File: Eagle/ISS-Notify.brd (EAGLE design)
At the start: 63.5 x 63.5 mm, 56 parts, among them J3 PROTOSPACE2, SW1 9077-1, U1 ATMEGA32U4, U2 MCP7940N, U3 TPS63001, U4 MCP73811, U5 TLC5971, U6 TLC5971, X1 8 MHz, X2 32.768 kHz

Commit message: test pin placement on board
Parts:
- added TESTCLOCK, TESTDATA, TESTGND, TESTSCL, TESTSDC, TESTVBAT: TESTPIN, ISS-Notify:TESTPIN
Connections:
- net GND: now also TESTGND.P$1
- net LED_CLK: now also TESTCLOCK.P$1
- net LED_DATA: now also TESTDATA.P$1
- net SCL: now also TESTSCL.P$1
- net SDA: now also TESTSDC.P$1
- net VBAT: now also TESTVBAT.P$1
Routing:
- net LED_CLK: track 10.9 -> 18.2 mm, vias 0 -> 2
- net SCL: track 27.4 -> 31.3 mm
- net LED_DATA: track 13.7 -> 17.4 mm
- net VBAT: track 16.9 -> 20.2 mm
- net SDA: track 26.5 -> 27.4 mm
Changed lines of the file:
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@@
 <attribute name="VALUE" x="48" y="62.5" size="1" layer="27" ratio="10" rot="R180"/>
 </element>
+<element name="TESTVBAT" library="ISS-Notify" package="TESTPIN" value="TESTPIN" x="44.5" y="58.3"/>
+<element name="TESTSCL" library="ISS-Notify" package="TESTPIN" value="TESTPIN" x="36.2" y="10"/>
+<element name="TESTSDC" library="ISS-Notify" package="TESTPIN" value="TESTPIN" x="46.1" y="13.4"/>
+<element name="TESTDATA" library="ISS-Notify" package="TESTPIN" value="TESTPIN" x="27.3" y="44.8"/>
+<element name="TESTCLOCK" library="ISS-Notify" package="TESTPIN" value="TESTPIN" x="27.3" y="47.1"/>
+<element name="TESTGND" library="ISS-Notify" package="TESTPIN" value="TESTPIN" x="57" y="8.9"/>
 </elements>
 <signals>
@@
 <wire x1="15.51" y1="55.625" x2="15.51" y2="53.69" width="0.254" layer="1"/>
 <wire x1="15.51" y1="53.69" x2="15.7" y2="53.5" width="0.254" layer="1"/>
+<contactref element="TESTGND" pad="P$1"/>
 <wire x1="13.46" y1="57.35" x2="13.4239" y2="57.3405" width="0" layer="19" extent="1-1"/>
 <wire x1="16.56" y1="57.35" x2="16.5354" y2="57.3405" width="0" layer="19" extent="1-1"/>
@@
 <wire x1="32.5" y1="24.7" x2="32.5" y2="25.7" width="0.254" layer="1"/>
 <wire x1="32.5" y1="25.7" x2="32.55" y2="25.75" width="0.254" layer="1"/>
+<contactref element="TESTSCL" pad="P$1"/>
+<wire x1="36.2" y1="10" x2="35.6" y2="10" width="0.254" layer="1"/>
+<wire x1="35.6" y1="10" x2="33.7" y2="11.9" width="0.254" layer="1"/>
+<wire x1="33.7" y1="11.9" x2="33.7" y2="12.1" width="0.254" layer="1"/>
+<wire x1="33.7" y1="12.1" x2="33.4" y2="12.4" width="0.254" layer="1"/>
 </signal>
 <signal name="SDA">
@@
 <wire x1="33.5" y1="14" x2="33.3" y2="13.8" width="0.254" layer="16"/>
 <wire x1="33.3" y1="13.8" x2="33.3" y2="13.3" width="0.254" layer="16"/>
+<contactref element="TESTSDC" pad="P$1"/>
+<wire x1="45.425" y1="12.775" x2="45.475" y2="12.775" width="0.254" layer="1"/>
+<wire x1="45.475" y1="12.775" x2="46.1" y2="13.4" width="0.254" layer="1"/>
 </signal>
 <signal name="N$10">
@@
 <wire x1="47.86" y1="58.2" x2="47.9" y2="59.3" width="0.6096" layer="1"/>
 <wire x1="47.9" y1="59.3" x2="47.9" y2="60.5" width="0.6096" layer="1"/>
+<contactref element="TESTVBAT" pad="P$1"/>
+<wire x1="47.81" y1="58.25" x2="44.75" y2="58.25" width="0.6096" layer="1"/>
+<wire x1="44.75" y1="58.25" x2="44.5" y2="58.3" width="0.6096" layer="1"/>
 </signal>
 <signal name="N$15">
@@
 <wire x1="34.385" y1="45.985" x2="34.3" y2="45.9" width="0.254" layer="1"/>
 <wire x1="34.3" y1="45.9" x2="32.9" y2="45.9" width="0.254" layer="1"/>
-<wire x1="32.9" y1="45.9" x2="29.4" y2="42.4" width="0.254" layer="1"/>
+<wire x1="32.9" y1="45.9" x2="30.55" y2="43.55" width="0.254" layer="1"/>
+<contactref element="TESTDATA" pad="P$1"/>
+<wire x1="30.55" y1="43.55" x2="29.4" y2="42.4" width="0.254" layer="1"/>
+<wire x1="27.3" y1="44.8" x2="29.3" y2="44.8" width="0.254" layer="1"/>
+<wire x1="29.3" y1="44.8" x2="30.55" y2="43.55" width="0.254" layer="1"/>
 </signal>
 <signal name="LED_CLK">
@@
 <contactref element="U1" pad="41"/>
 <wire x1="30.15" y1="37.75" x2="30.15" y2="42.15" width="0.254" layer="1"/>
-<wire x1="30.15" y1="42.15" x2="33.3" y2="45.3" width="0.254" layer="1"/>
+<wire x1="30.15" y1="42.15" x2="31.35" y2="43.35" width="0.254" layer="1"/>
+<wire x1="31.35" y1="43.35" x2="33.3" y2="45.3" width="0.254" layer="1"/>
 <wire x1="33.3" y1="45.3" x2="35.265" y2="45.3" width="0.254" layer="1"/>
 <wire x1="35.265" y1="45.3" x2="35.3" y2="45.335" width="0.254" layer="1"/>
+<contactref element="TESTCLOCK" pad="P$1"/>
+<wire x1="27.3" y1="47.1" x2="30.6" y2="47.1" width="0.254" layer="1"/>
+<wire x1="30.6" y1="47.1" x2="31.3" y2="46.4" width="0.254" layer="1"/>
+<via x="31.3" y="46.4" extent="1-16" drill="0.36"/>
+<wire x1="31.3" y1="46.4" x2="31.3" y2="43.4" width="0.254" layer="16"/>
+<wire x1="31.3" y1="43.4" x2="31.35" y2="43.35" width="0.254" layer="16"/>
+<via x="31.35" y="43.35" extent="1-16" drill="0.36"/>
 </signal>
 <signal name="N$17">

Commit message: incrament board version on screen
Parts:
- U$5: value V0.3 -> V0.4
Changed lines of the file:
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@@
 <attribute name="VALUE" x="50.36" y="7.666" size="1" layer="27" ratio="10" rot="R90"/>
 </element>
-<element name="U$5" library="ISS-Notify" package="LOGO" value="V0.3" x="40.7" y="35.5"/>
+<element name="U$5" library="ISS-Notify" package="LOGO" value="V0.4" x="40.7" y="35.5"/>
 <element name="C17" library="rcl_custom" package="0603-C-NOSILK" value="1 uF" x="47.2" y="60.5" smashed="yes" rot="R180">
 <attribute name="NAME" x="51" y="61.15" size="0.8" layer="25" font="vector" ratio="20" rot="R180"/>

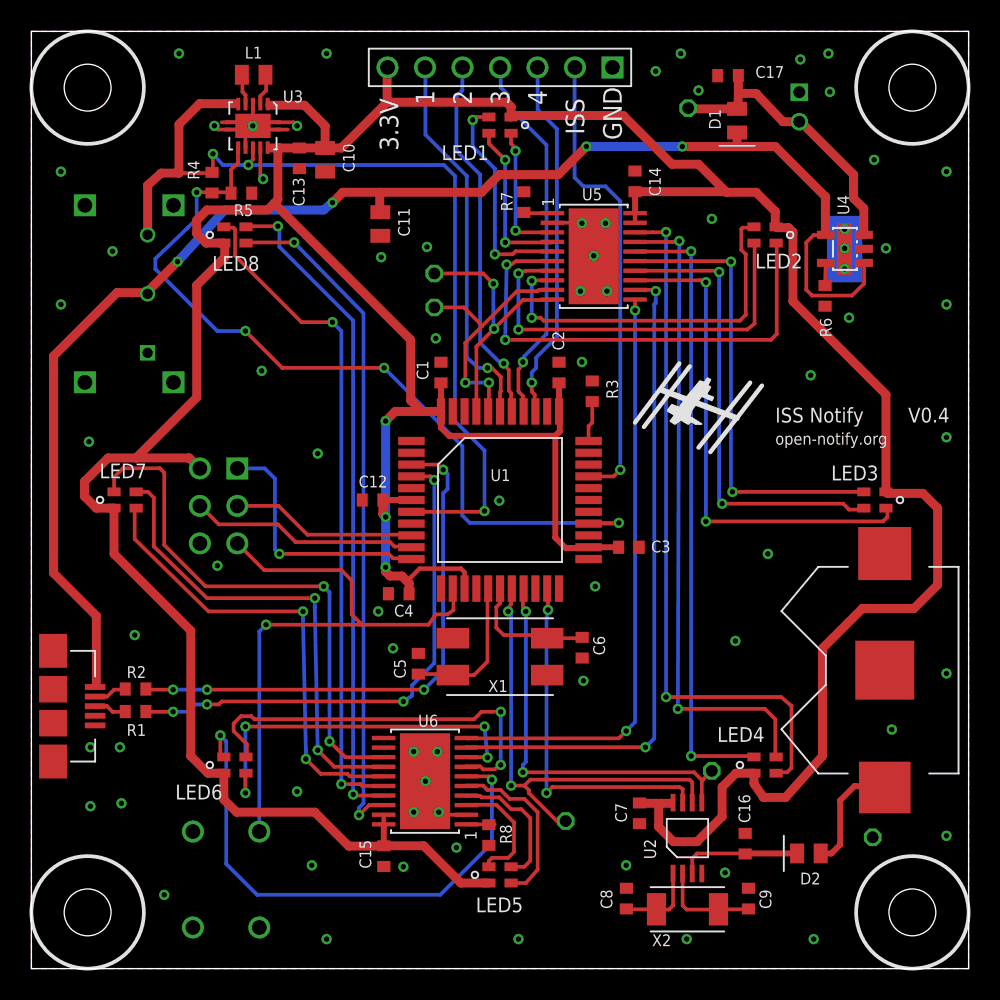
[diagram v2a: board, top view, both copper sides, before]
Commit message: fixed annoying bolt landing, moved a via or two
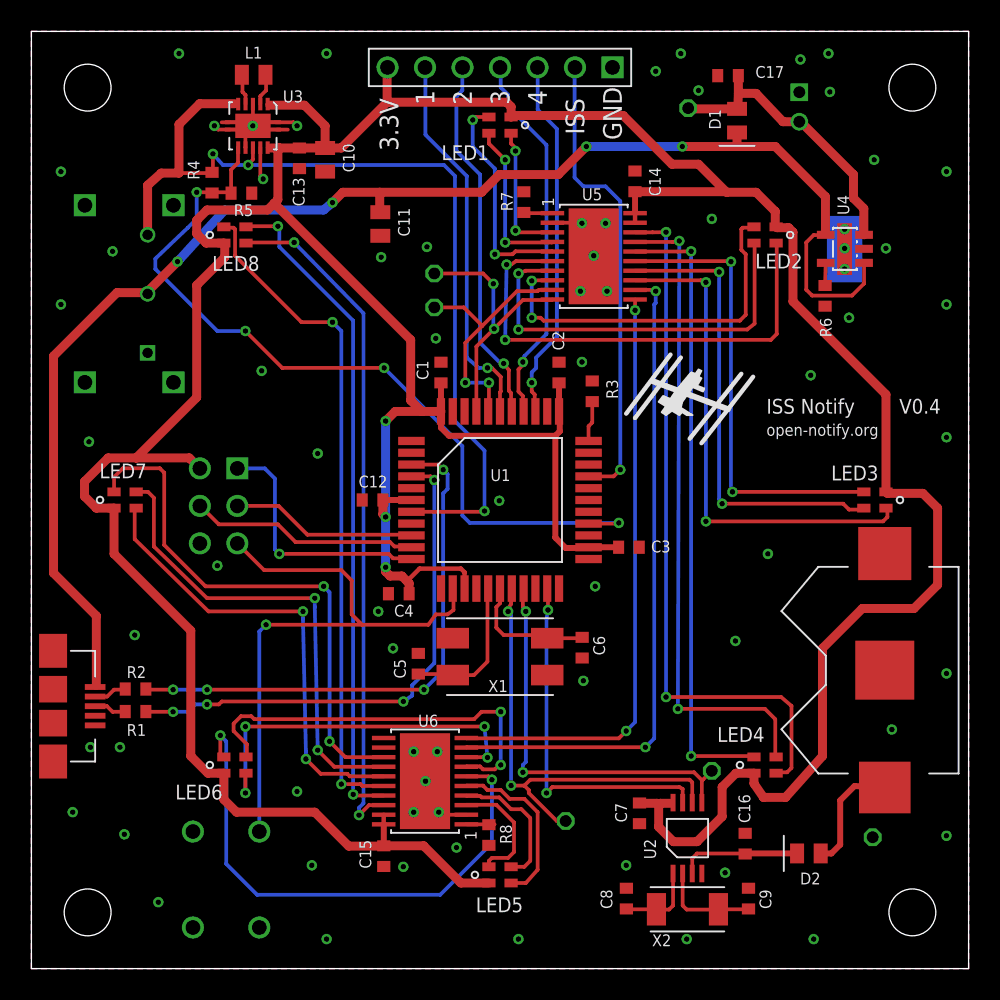
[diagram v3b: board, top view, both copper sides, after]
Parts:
- U$1, U$2, U$3, U$4: value _4-BARE_MOUNTING_HOLE/.300 -> _4-BARE_MOUNTING_HOLE/.250; device ISS-Notify:_4/.300-BARE+STD_NUT_OR_STAR_WASHER -> ISS-Notify:_4/.250-BARE+STD_WASHER
- moved U$5 0.85 mm to (40.1, 36.1)
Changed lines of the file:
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@@
 <layer number="39" name="tKeepout" color="4" fill="11" visible="no" active="yes"/>
 <layer number="40" name="bKeepout" color="1" fill="11" visible="no" active="yes"/>
-<layer number="41" name="tRestrict" color="4" fill="10" visible="no" active="yes"/>
+<layer number="41" name="tRestrict" color="4" fill="10" visible="yes" active="yes"/>
 <layer number="42" name="bRestrict" color="1" fill="10" visible="no" active="yes"/>
 <layer number="43" name="vRestrict" color="2" fill="10" visible="no" active="yes"/>
@@
 <layer number="46" name="Milling" color="3" fill="1" visible="no" active="yes"/>
 <layer number="47" name="Measures" color="7" fill="1" visible="no" active="yes"/>
-<layer number="48" name="Document" color="7" fill="1" visible="yes" active="yes"/>
+<layer number="48" name="Document" color="7" fill="1" visible="no" active="yes"/>
 <layer number="49" name="Reference" color="7" fill="1" visible="no" active="yes"/>
 <layer number="50" name="dxf" color="7" fill="1" visible="no" active="no"/>
-<layer number="51" name="tDocu" color="7" fill="1" visible="yes" active="yes"/>
+<layer number="51" name="tDocu" color="7" fill="1" visible="no" active="yes"/>
 <layer number="52" name="bDocu" color="7" fill="1" visible="no" active="yes"/>
 <layer number="53" name="tGND_GNDA" color="7" fill="1" visible="no" active="no"/>
@@
 <attribute name="NAME" x="17.008" y="3.364" size="1.27" layer="26" font="vector" ratio="20" rot="MR90"/>
 </element>
-<element name="U$1" library="ISS-Notify" package="_4/.300-BARE+STD_NUT_OR_STAR_WASHER" value="_4-BARE_MOUNTING_HOLE/.300" x="3.81" y="59.69" smashed="yes">
+<element name="U$1" library="ISS-Notify" package="_4/.250-BARE+STD_WASHER" value="_4-BARE_MOUNTING_HOLE/.250" x="3.81" y="59.69" smashed="yes">
 <attribute name="VALUE" x="6.985" y="56.515" size="1.27" layer="27"/>
 </element>
-<element name="U$2" library="ISS-Notify" package="_4/.300-BARE+STD_NUT_OR_STAR_WASHER" value="_4-BARE_MOUNTING_HOLE/.300" x="59.69" y="59.69" smashed="yes">
+<element name="U$2" library="ISS-Notify" package="_4/.250-BARE+STD_WASHER" value="_4-BARE_MOUNTING_HOLE/.250" x="59.69" y="59.69" smashed="yes">
 <attribute name="VALUE" x="62.865" y="56.515" size="1.27" layer="27"/>
 </element>
-<element name="U$3" library="ISS-Notify" package="_4/.300-BARE+STD_NUT_OR_STAR_WASHER" value="_4-BARE_MOUNTING_HOLE/.300" x="59.69" y="3.81" smashed="yes">
+<element name="U$3" library="ISS-Notify" package="_4/.250-BARE+STD_WASHER" value="_4-BARE_MOUNTING_HOLE/.250" x="59.69" y="3.81" smashed="yes">
 <attribute name="VALUE" x="62.865" y="0.635" size="1.27" layer="27"/>
 </element>
-<element name="U$4" library="ISS-Notify" package="_4/.300-BARE+STD_NUT_OR_STAR_WASHER" value="_4-BARE_MOUNTING_HOLE/.300" x="3.81" y="3.81" smashed="yes">
+<element name="U$4" library="ISS-Notify" package="_4/.250-BARE+STD_WASHER" value="_4-BARE_MOUNTING_HOLE/.250" x="3.81" y="3.81" smashed="yes">
 <attribute name="VALUE" x="6.985" y="0.635" size="1.27" layer="27"/>
 </element>
@@
 <attribute name="VALUE" x="50.36" y="7.666" size="1" layer="27" ratio="10" rot="R90"/>
 </element>
-<element name="U$5" library="ISS-Notify" package="LOGO" value="V0.4" x="40.7" y="35.5"/>
+<element name="U$5" library="ISS-Notify" package="LOGO" value="V0.4" x="40.1" y="36.1"/>
 <element name="C17" library="rcl_custom" package="0603-C-NOSILK" value="1 uF" x="47.2" y="60.5" smashed="yes" rot="R180">
 <attribute name="NAME" x="51" y="61.15" size="0.8" layer="25" font="vector" ratio="20" rot="R180"/>
@@
 <via x="4" y="15" extent="1-16" drill="0.36"/>
 <via x="6" y="15" extent="1-16" drill="0.36"/>
-<via x="4" y="11" extent="1-16" drill="0.36"/>
+<via x="2.8" y="10.6" extent="1-16" drill="0.36"/>
 <via x="19" y="7" extent="1-16" drill="0.36"/>
 <via x="18" y="12" extent="1-16" drill="0.36"/>
@@
 <via x="19.4" y="34.9" extent="1-16" drill="0.36"/>
 <via x="7" y="22.6" extent="1-16" drill="0.36"/>
-<via x="6.1" y="11.2" extent="1-16" drill="0.36"/>
+<via x="6.3" y="9.1" extent="1-16" drill="0.36"/>
 <via x="38.1" y="48.3" extent="1-16" drill="0.36"/>
 <via x="57.1" y="54.8" extent="1-16" drill="0.36"/>
@@
 <via x="62" y="20" extent="1-16" drill="0.36"/>
 <via x="62" y="9" extent="1-16" drill="0.36"/>
-<via x="9" y="5" extent="1-16" drill="0.36"/>
+<via x="8.6" y="4.5" extent="1-16" drill="0.36"/>
 <contactref element="C11" pad="2"/>
 <contactref element="C17" pad="2"/>
@@
 </signal>
 </signals>
-<errors>
-</errors>
 </board>
 </drawing>

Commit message: Fixed L1 packages, changed USB header. Passes ERC, DRC, rats. Ship it.
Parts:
- removed USB: CON_USB-MICRO-6GND, ISS-Notify:USBMICROSMT
- added J1: ZX62D-B-5P8, con-hirose-microusb:ZX62D-B-5P8
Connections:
- net GND: now also J1.P$1, J1.P$2, J1.P$3, J1.P$4, J1.P5, U1.42; no longer USB.5
- net N$4: now also J1.P3; no longer USB.D+
- net N$5: now also J1.P2; no longer USB.D-
- net VUSB: now also J1.P1; no longer USB.VUSB
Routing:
- net VUSB: track 99.1 -> 100.6 mm
- net GND: track 16.2 -> 16.3 mm, vias 67 -> 65

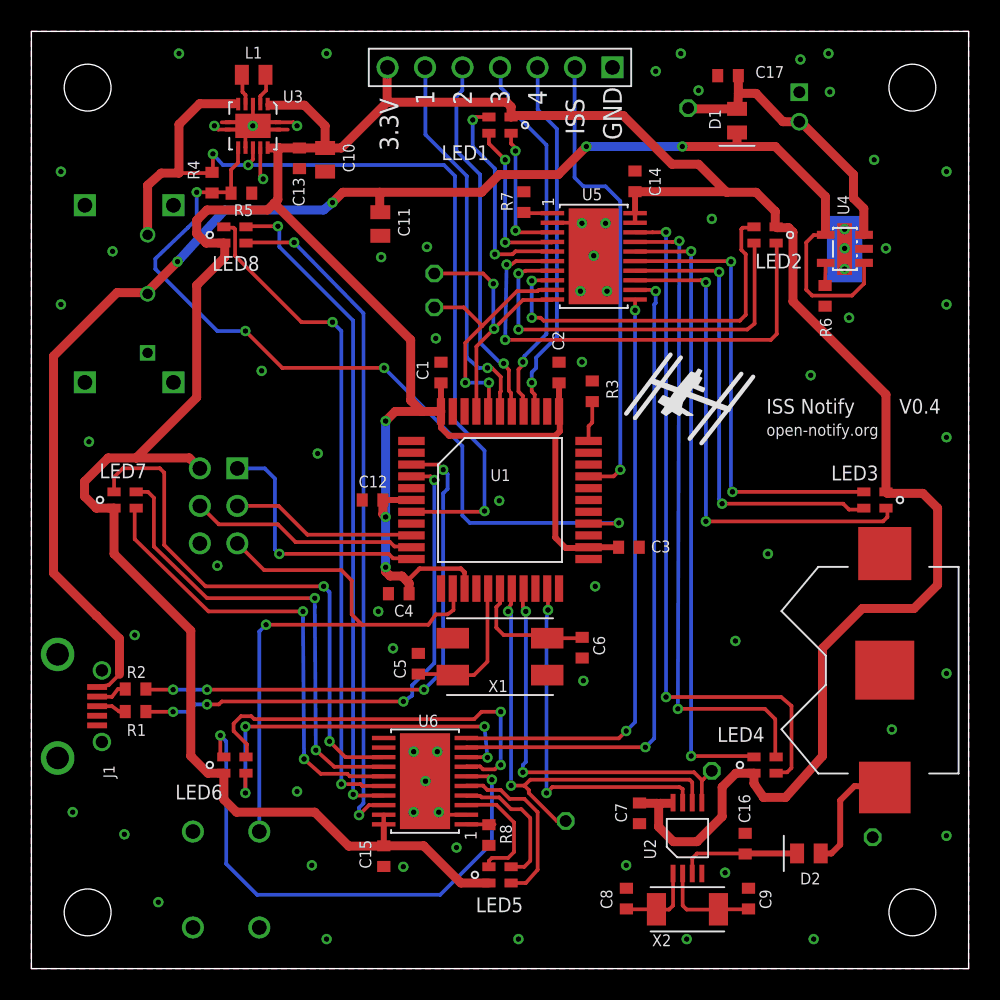
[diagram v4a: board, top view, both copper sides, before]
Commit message: Added fiducials per Screaming Circuits blog postw.
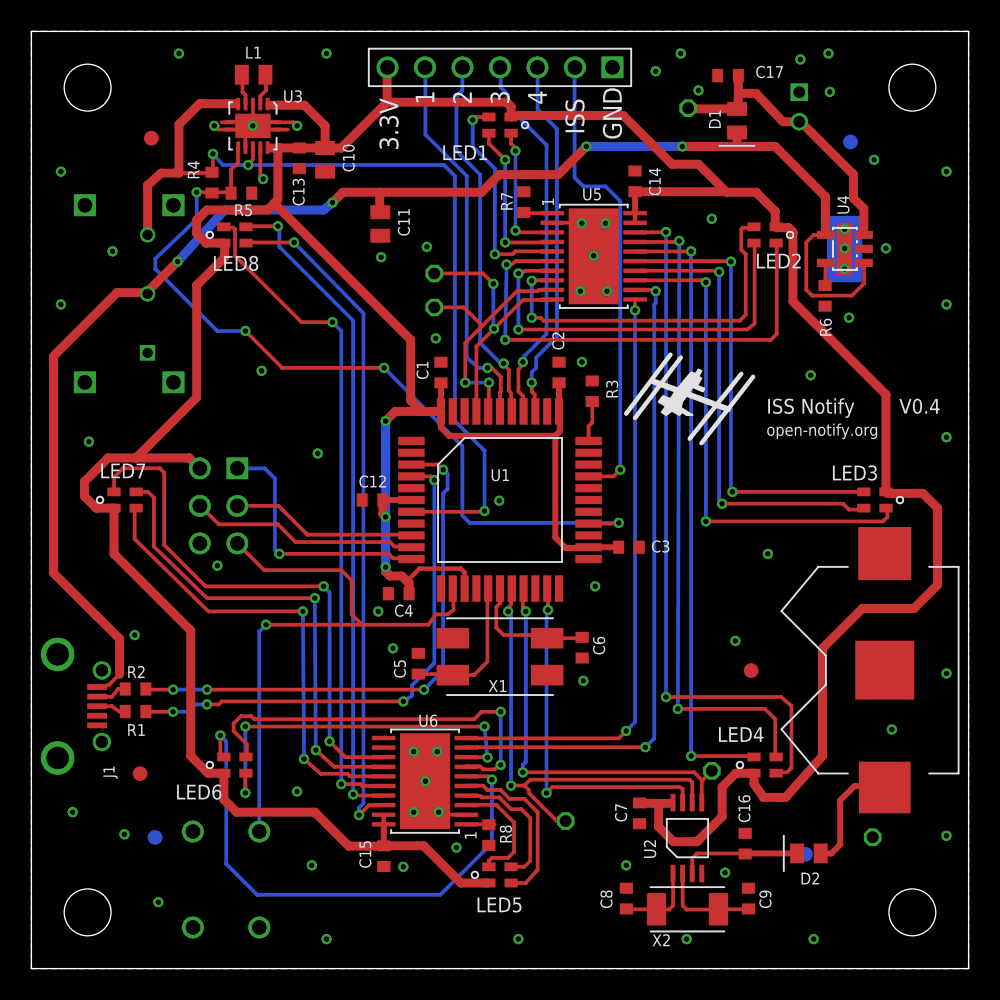
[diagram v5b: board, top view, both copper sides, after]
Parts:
- added U$10, U$11, U$6, U$7, U$8, U$9: FIDUCIAL, adafruit:FIDUCIAL_1MM
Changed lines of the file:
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@@
 <setting verticaltext="up"/>
 </settings>
-<grid distance="0.005" unitdist="inch" unit="inch" style="dots" multiple="1" display="yes" altdistance="0.025" altunitdist="inch" altunit="inch"/>
+<grid distance="4.75" unitdist="mm" unit="mm" style="dots" multiple="1" display="yes" altdistance="0.025" altunitdist="inch" altunit="inch"/>
 <layers>
 <layer number="1" name="Top" color="4" fill="1" visible="yes" active="yes"/>
@@
 <layer number="54" name="bGND_GNDA" color="7" fill="1" visible="no" active="no"/>
 <layer number="56" name="wert" color="7" fill="1" visible="no" active="no"/>
+<layer number="57" name="tCAD" color="7" fill="1" visible="no" active="no"/>
 <layer number="59" name="Invisible" color="7" fill="1" visible="no" active="yes"/>
 <layer number="61" name="stand" color="7" fill="1" visible="no" active="yes"/>
@@
 <layer number="132" name="bMask" color="7" fill="1" visible="no" active="yes"/>
 <layer number="144" name="Drill_legend" color="7" fill="1" visible="no" active="yes"/>
+<layer number="150" name="Notes" color="7" fill="1" visible="no" active="yes"/>
 <layer number="151" name="HeatSink" color="7" fill="1" visible="no" active="yes"/>
 <layer number="152" name="_bDocu" color="7" fill="1" visible="no" active="yes"/>
+<layer number="153" name="FabDoc1" color="6" fill="1" visible="no" active="no"/>
+<layer number="154" name="FabDoc2" color="2" fill="1" visible="no" active="no"/>
+<layer number="155" name="FabDoc3" color="7" fill="15" visible="no" active="no"/>
 <layer number="199" name="Contour" color="7" fill="1" visible="no" active="yes"/>
 <layer number="200" name="200bmp" color="7" fill="1" visible="no" active="yes"/>
@@
 <element name="TESTGND" library="ISS-Notify" package="TESTPIN" value="TESTPIN" x="57" y="8.9"/>
 <element name="J1" library="con-hirose-microusb" package="ZX62D-B-5P8" value="ZX62D-B-5P8" x="1.778" y="17.78" rot="R270"/>
+<element name="U$6" library="adafruit" package="FIDUCIAL_1MM" value="FIDUCIAL" x="8.128" y="56.261"/>
+<element name="U$7" library="adafruit" package="FIDUCIAL_1MM" value="FIDUCIAL" x="8.382" y="8.89" rot="MR0"/>
+<element name="U$8" library="adafruit" package="FIDUCIAL_1MM" value="FIDUCIAL" x="7.366" y="13.208"/>
+<element name="U$9" library="adafruit" package="FIDUCIAL_1MM" value="FIDUCIAL" x="48.768" y="20.193"/>
+<element name="U$10" library="adafruit" package="FIDUCIAL_1MM" value="FIDUCIAL" x="55.499" y="56.007" rot="MR0"/>
+<element name="U$11" library="adafruit" package="FIDUCIAL_1MM" value="FIDUCIAL" x="52.451" y="7.747" rot="MR0"/>
 </elements>
 <signals>
